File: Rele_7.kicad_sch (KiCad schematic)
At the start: 5 parts, among them J13 Rele_7, K2 SRD-05VDC-SL-C, Q10 PMBT3904,235

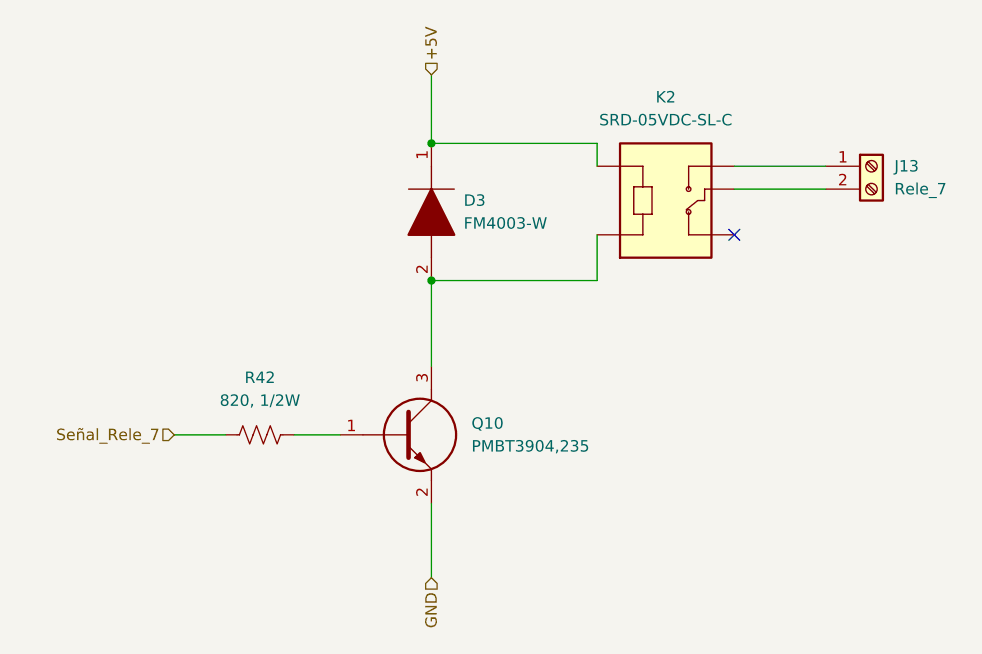
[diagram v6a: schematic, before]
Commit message: Se modificaron algunos componentes, según disponibilidad
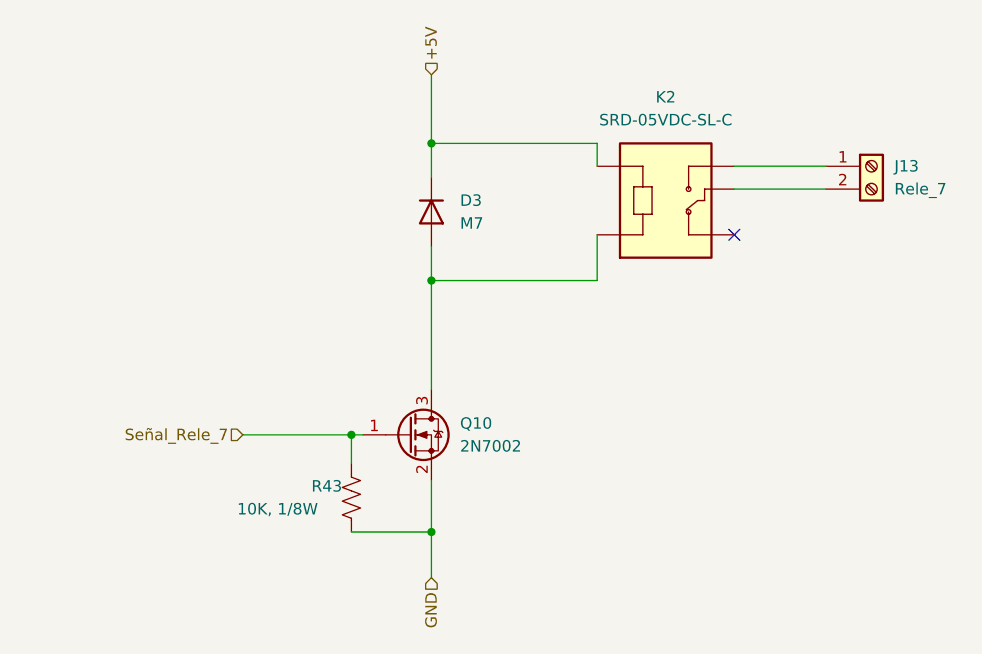
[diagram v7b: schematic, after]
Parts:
- removed D3: FM4003-W, FM4003W:DIOM5025X231N, symbol FM4003-W:FM4003-W
- removed Q10: PMBT3904,235, PMBT3904,235:SOT95P230X110-3N, symbol PMBT3904,235:PMBT3904,235
- removed R42: 820, 1/2W, Resistor_SMD:R_0805_2012Metric, symbol Device:R_US
- added D3: M7, Diode_SMD:D_SMA, symbol Device:D
- added Q10: 2N7002, Package_TO_SOT_SMD:SOT-23, symbol Transistor_FET:2N7002
- added R43: 10K, 1/8W, Resistor_SMD:R_0805_2012Metric, symbol Device:R_US
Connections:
- net +5V: now also D3.1 (K)
- net GND: now also Q10.2 (S), R43.2
- net Señal_Rele_7: now also Q10.1 (G), R43.1
- net at K2.A2: now also D3.2 (A), Q10.3 (D)
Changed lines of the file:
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@@
 (kicad_sch (version 20211123) (generator eeschema)
   (paper "A4")
-  (junction (at 144.145 75.565) (diameter 0) (color 0 0 0 0)
+  (junction (at 144.145 118.745) (diameter 0) (color 0 0 0 0)
+  )
+  (junction (at 135.255 107.95) (diameter 0) (color 0 0 0 0)
   )
   (junction (at 144.145 90.805) (diameter 0) (color 0 0 0 0)
   )
+  (junction (at 144.145 75.565) (diameter 0) (color 0 0 0 0)
+  )
   (no_connect (at 177.8 85.725))
+  (wire (pts (xy 144.145 75.565) (xy 144.145 79.375))
+    (stroke (width 0) (type default) (color 0 0 0 0))
+  )
+  (wire (pts (xy 135.255 107.95) (xy 135.255 111.125))
+    (stroke (width 0) (type default) (color 0 0 0 0))
+  )
   (wire (pts (xy 144.145 90.805) (xy 162.56 90.805))
     (stroke (width 0) (type default) (color 0 0 0 0))
   )
-  (wire (pts (xy 115.57 107.95) (xy 121.285 107.95))
+  (wire (pts (xy 123.19 107.95) (xy 135.255 107.95))
     (stroke (width 0) (type default) (color 0 0 0 0))
   )
-  (wire (pts (xy 128.905 107.95) (xy 133.985 107.95))
+  (wire (pts (xy 135.255 107.95) (xy 136.525 107.95))
+    (stroke (width 0) (type default) (color 0 0 0 0))
+  )
+  (wire (pts (xy 144.145 118.745) (xy 144.145 123.825))
     (stroke (width 0) (type default) (color 0 0 0 0))
   )
@@
     (stroke (width 0) (type default) (color 0 0 0 0))
   )
-  (wire (pts (xy 144.145 115.57) (xy 144.145 123.825))
+  (wire (pts (xy 144.145 86.995) (xy 144.145 90.805))
+    (stroke (width 0) (type default) (color 0 0 0 0))
+  )
+  (wire (pts (xy 144.145 113.03) (xy 144.145 118.745))
     (stroke (width 0) (type default) (color 0 0 0 0))
   )
@@
     (stroke (width 0) (type default) (color 0 0 0 0))
   )
+  (wire (pts (xy 135.255 118.745) (xy 144.145 118.745))
+    (stroke (width 0) (type default) (color 0 0 0 0))
+  )
   (wire (pts (xy 144.145 67.945) (xy 144.145 75.565))
     (stroke (width 0) (type default) (color 0 0 0 0))
   )
-  (wire (pts (xy 144.145 90.805) (xy 144.145 100.33))
+  (wire (pts (xy 144.145 90.805) (xy 144.145 102.87))
     (stroke (width 0) (type default) (color 0 0 0 0))
   )
-  (hierarchical_label "Señal_Rele_7" (shape input) (at 115.57 107.95 180)
+  (hierarchical_label "Señal_Rele_7" (shape input) (at 123.19 107.95 180)
     (effects (font (size 1.27 1.27)) (justify right))
   )
@@
     (effects (font (size 1.27 1.27)) (justify right))
   )
-  (symbol (lib_id "Device:R_US") (at 125.095 107.95 90) (unit 1)
+  (symbol (lib_id "Transistor_FET:2N7002") (at 141.605 107.95 0) (unit 1)
     (in_bom yes) (on_board yes) (fields_autoplaced)
-    (property "Reference" "R42" (id 0) (at 125.095 101.6 90))
-    (property "Value" "820, 1/2W" (id 1) (at 125.095 104.14 90))
-    (property "Footprint" "Resistor_SMD:R_0805_2012Metric" (id 2) (at 125.349 106.934 90)
-      (effects (font (size 1.27 1.27)) hide)
-    )
-    (property "Datasheet" "~" (id 3) (at 125.095 107.95 0)
-      (effects (font (size 1.27 1.27)) hide)
-    )
-    (pin "1")
-    (pin "2")
-  )
-  (symbol (lib_id "FM4003-W:FM4003-W") (at 144.145 75.565 270) (unit 1)
-    (in_bom yes) (on_board yes) (fields_autoplaced)
-    (property "Reference" "D3" (id 0) (at 147.7264 81.9149 90)
+    (property "Reference" "Q10" (id 0) (at 147.32 106.6799 0)
       (effects (font (size 1.27 1.27)) (justify left))
     )
-    (property "Value" "FM4003-W" (id 1) (at 147.7264 84.4549 90)
+    (property "Value" "2N7002" (id 1) (at 147.32 109.2199 0)
       (effects (font (size 1.27 1.27)) (justify left))
     )
-    (property "Footprint" "FM4003W:DIOM5025X231N" (id 2) (at 144.145 86.995 0)
-      (effects (font (size 1.27 1.27)) (justify left) hide)
+    (property "Footprint" "Package_TO_SOT_SMD:SOT-23" (id 2) (at 146.685 109.855 0)
+      (effects (font (size 1.27 1.27) italic) (justify left) hide)
     )
-    (property "Datasheet" "https://componentsearchengine.com/Datasheets/1/FM4003-W.pdf" (id 3) (at 141.605 86.995 0)
-      (effects (font (size 1.27 1.27)) (justify left) hide)
-    )
-    (property "Description" "Rectifiers 1A 200V GP" (id 4) (at 139.065 86.995 0)
-      (effects (font (size 1.27 1.27)) (justify left) hide)
-    )
-    (property "Height" "2.31" (id 5) (at 136.525 86.995 0)
-      (effects (font (size 1.27 1.27)) (justify left) hide)
-    )
-    (property "Manufacturer_Name" "Rectron" (id 6) (at 133.985 86.995 0)
-      (effects (font (size 1.27 1.27)) (justify left) hide)
-    )
-    (property "Manufacturer_Part_Number" "FM4003-W" (id 7) (at 131.445 86.995 0)
-      (effects (font (size 1.27 1.27)) (justify left) hide)
-    )
-    (property "Mouser Part Number" "583-FM4003-W" (id 8) (at 128.905 86.995 0)
-      (effects (font (size 1.27 1.27)) (justify left) hide)
-    )
-    (property "Mouser Price/Stock" "https://www.mouser.co.uk/ProductDetail/Rectron/FM4003-W/?qs=5h8Q3Z7TNRlJu6QU92Ho0w%3D%3D" (id 9) (at 126.365 86.995 0)
-      (effects (font (size 1.27 1.27)) (justify left) hide)
-    )
-    (property "Arrow Part Number" "FM4003-W" (id 10) (at 123.825 86.995 0)
-      (effects (font (size 1.27 1.27)) (justify left) hide)
-    )
-    (property "Arrow Price/Stock" "https://www.arrow.com/en/products/fm4003-w/rectron" (id 11) (at 121.285 86.995 0)
-      (effects (font (size 1.27 1.27)) (justify left) hide)
-    )
-    (property "Mouser Testing Part Number" "" (id 12) (at 118.745 86.995 0)
-      (effects (font (size 1.27 1.27)) (justify left) hide)
-    )
-    (property "Mouser Testing Price/Stock" "" (id 13) (at 116.205 86.995 0)
+    (property "Datasheet" "https://www.onsemi.com/pub/Collateral/NDS7002A-D.PDF" (id 3) (at 141.605 107.95 0)
       (effects (font (size 1.27 1.27)) (justify left) hide)
     )
     (pin "1")
     (pin "2")
+    (pin "3")
   )
   (symbol (lib_id "Connector:Screw_Terminal_01x02") (at 193.04 78.105 0) (unit 1)
@@
     )
     (property "Datasheet" "~" (id 3) (at 193.04 78.105 0)
+      (effects (font (size 1.27 1.27)) hide)
+    )
+    (pin "1")
+    (pin "2")
+  )
+  (symbol (lib_id "Device:D") (at 144.145 83.185 270) (unit 1)
+    (in_bom yes) (on_board yes) (fields_autoplaced)
+    (property "Reference" "D3" (id 0) (at 147.32 81.9149 90)
+      (effects (font (size 1.27 1.27)) (justify left))
+    )
+    (property "Value" "M7" (id 1) (at 147.32 84.4549 90)
+      (effects (font (size 1.27 1.27)) (justify left))
+    )
+    (property "Footprint" "Diode_SMD:D_SMA" (id 2) (at 144.145 83.185 0)
+      (effects (font (size 1.27 1.27)) hide)
+    )
+    (property "Datasheet" "~" (id 3) (at 144.145 83.185 0)
+      (effects (font (size 1.27 1.27)) hide)
+    )
+    (pin "1")
+    (pin "2")
+  )
+  (symbol (lib_id "Device:R_US") (at 135.255 114.935 0) (unit 1)
+    (in_bom yes) (on_board yes)
+    (property "Reference" "R43" (id 0) (at 130.81 113.665 0)
+      (effects (font (size 1.27 1.27)) (justify left))
+    )
+    (property "Value" "10K, 1/8W" (id 1) (at 122.555 116.205 0)
+      (effects (font (size 1.27 1.27)) (justify left))
+    )
+    (property "Footprint" "Resistor_SMD:R_0805_2012Metric" (id 2) (at 136.271 115.189 90)
+      (effects (font (size 1.27 1.27)) hide)
+    )
+    (property "Datasheet" "~" (id 3) (at 135.255 114.935 0)
       (effects (font (size 1.27 1.27)) hide)
     )
@@
     (pin "NO")
   )
-  (symbol (lib_id "PMBT3904,235:PMBT3904,235") (at 133.985 107.95 0) (unit 1)
-    (in_bom yes) (on_board yes) (fields_autoplaced)
-    (property "Reference" "Q10" (id 0) (at 148.59 106.6799 0)
-      (effects (font (size 1.27 1.27)) (justify left))
-    )
-    (property "Value" "PMBT3904,235" (id 1) (at 148.59 109.2199 0)
-      (effects (font (size 1.27 1.27)) (justify left))
-    )
-    (property "Footprint" "PMBT3904,235:SOT95P230X110-3N" (id 2) (at 147.955 111.76 0)
-      (effects (font (size 1.27 1.27)) (justify left) hide)
-    )
-    (property "Datasheet" "https://assets.nexperia.com/documents/data-sheet/PMBT3904.pdf" (id 3) (at 147.955 114.3 0)
-      (effects (font (size 1.27 1.27)) (justify left) hide)
-    )
-    (property "Description" "PMBT3904 - NPN switching transistor" (id 4) (at 147.955 116.84 0)
-      (effects (font (size 1.27 1.27)) (justify left) hide)
-    )
-    (property "Height" "1.1" (id 5) (at 147.955 119.38 0)
-      (effects (font (size 1.27 1.27)) (justify left) hide)
-    )
-    (property "Manufacturer_Name" "Nexperia" (id 6) (at 147.955 121.92 0)
-      (effects (font (size 1.27 1.27)) (justify left) hide)
-    )
-    (property "Manufacturer_Part_Number" "PMBT3904,235" (id 7) (at 147.955 124.46 0)
-      (effects (font (size 1.27 1.27)) (justify left) hide)
-    )
-    (property "Mouser Part Number" "771-PMBT3904235" (id 8) (at 147.955 127 0)
-      (effects (font (size 1.27 1.27)) (justify left) hide)
-    )
-    (property "Mouser Price/Stock" "https://www.mouser.co.uk/ProductDetail/Nexperia/PMBT3904235?qs=LOCUfHb8d9uziIfl4fmvZg%3D%3D" (id 9) (at 147.955 129.54 0)
-      (effects (font (size 1.27 1.27)) (justify left) hide)
-    )
-    (property "Arrow Part Number" "PMBT3904,235" (id 10) (at 147.955 132.08 0)
-      (effects (font (size 1.27 1.27)) (justify left) hide)
-    )
-    (property "Arrow Price/Stock" "https://www.arrow.com/en/products/pmbt3904235/nexperia?region=nac" (id 11) (at 147.955 134.62 0)
-      (effects (font (size 1.27 1.27)) (justify left) hide)
-    )
-    (property "Mouser Testing Part Number" "" (id 12) (at 147.955 137.16 0)
-      (effects (font (size 1.27 1.27)) (justify left) hide)
-    )
-    (property "Mouser Testing Price/Stock" "" (id 13) (at 147.955 139.7 0)
-      (effects (font (size 1.27 1.27)) (justify left) hide)
-    )
-    (pin "1")
-    (pin "2")
-    (pin "3")
-  )
 )

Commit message: Finalización de rerouteo de PCB.
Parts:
- added J44: Pin GND, Connector_PinHeader_2.54mm:PinHeader_1x01_P2.54mm_Vertical, symbol Connector_Generic:Conn_01x01
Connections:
- net GND: now also J44.1 (Pin_1)
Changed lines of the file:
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@@
+    (stroke (width 0) (type default) (color 0 0 0 0))
+  )
+  (wire (pts (xy 144.145 118.745) (xy 148.59 118.745))
     (stroke (width 0) (type default) (color 0 0 0 0))
   )
@@
     (pin "3")
   )
+  (symbol (lib_id "Connector_Generic:Conn_01x01") (at 153.67 118.745 0) (unit 1)
+    (in_bom yes) (on_board yes) (fields_autoplaced)
+    (property "Reference" "J44" (id 0) (at 156.9212 117.4749 0)
+      (effects (font (size 1.27 1.27)) (justify left))
+    )
+    (property "Value" "Pin GND" (id 1) (at 156.9212 120.0149 0)
+      (effects (font (size 1.27 1.27)) (justify left))
+    )
+    (property "Footprint" "Connector_PinHeader_2.54mm:PinHeader_1x01_P2.54mm_Vertical" (id 2) (at 153.67 118.745 0)
+      (effects (font (size 1.27 1.27)) hide)
+    )
+    (property "Datasheet" "~" (id 3) (at 153.67 118.745 0)
+      (effects (font (size 1.27 1.27)) hide)
+    )
+    (pin "1")
+  )
   (symbol (lib_id "Connector:Screw_Terminal_01x02") (at 193.04 78.105 0) (unit 1)
